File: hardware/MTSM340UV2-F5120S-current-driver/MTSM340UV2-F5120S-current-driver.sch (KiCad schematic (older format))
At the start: 9 parts

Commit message: course layout done
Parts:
- removed C?: 10V 1uF, symbol Device:C
- removed C?: 25V 3.3uF, symbol Device:C
- removed C?: 6V 1uF, symbol Device:C
- removed D?: 20V 1A, symbol Device:D_Schottky
- removed J?: LED, symbol Connector:Conn_01x02_Female
- removed L?: 22uH, symbol pspice:INDUCTOR
- removed R?: 40.2k, symbol Device:R
- removed R?: 0.665, symbol Device:R
- removed U?: LM3407MY, Package_SO:MSOP-8-1EP_3x3mm_P0.65mm_EP1.73x1.85mm_ThermalVias, symbol Regulator_Switching:LM3407MY
- added C10: 5600pF, Capacitor_SMD:C_0402_1005Metric, symbol Device:C
- added C11: 0.1uF, Capacitor_SMD:C_0402_1005Metric, symbol Device:C
- added C12: 22uF, Capacitor_SMD:C_0805_2012Metric, symbol Device:C
- added C8, C9: 2.2uF, Capacitor_SMD:C_0603_1608Metric, symbol Device:C
- added J1: LED0, Connector_PinHeader_2.54mm:PinHeader_1x02_P2.54mm_Vertical, symbol Connector:Conn_01x02_Female
- added J10: LED8, Connector_PinHeader_2.54mm:PinHeader_1x02_P2.54mm_Vertical, symbol Connector:Conn_01x02_Female
- added J11: LED9, Connector_PinHeader_2.54mm:PinHeader_1x02_P2.54mm_Vertical, symbol Connector:Conn_01x02_Female
- added J12: LED10, Connector_PinHeader_2.54mm:PinHeader_1x02_P2.54mm_Vertical, symbol Connector:Conn_01x02_Female
- added J13: LED11, Connector_PinHeader_2.54mm:PinHeader_1x02_P2.54mm_Vertical, symbol Connector:Conn_01x02_Female
- added J14: LED12, Connector_PinHeader_2.54mm:PinHeader_1x02_P2.54mm_Vertical, symbol Connector:Conn_01x02_Female
- added J15: LED13, Connector_PinHeader_2.54mm:PinHeader_1x02_P2.54mm_Vertical, symbol Connector:Conn_01x02_Female
- added J16: LED14, Connector_PinHeader_2.54mm:PinHeader_1x02_P2.54mm_Vertical, symbol Connector:Conn_01x02_Female
- added J17: LED15, Connector_PinHeader_2.54mm:PinHeader_1x02_P2.54mm_Vertical, symbol Connector:Conn_01x02_Female
- added J18: LED16, Connector_PinHeader_2.54mm:PinHeader_1x02_P2.54mm_Vertical, symbol Connector:Conn_01x02_Female
- added J19: LED17, Connector_PinHeader_2.54mm:PinHeader_1x02_P2.54mm_Vertical, symbol Connector:Conn_01x02_Female
- added J2: LED1, Connector_PinHeader_2.54mm:PinHeader_1x02_P2.54mm_Vertical, symbol Connector:Conn_01x02_Female
- added J20: LED18, Connector_PinHeader_2.54mm:PinHeader_1x02_P2.54mm_Vertical, symbol Connector:Conn_01x02_Female
- added J21: LED19, Connector_PinHeader_2.54mm:PinHeader_1x02_P2.54mm_Vertical, symbol Connector:Conn_01x02_Female
- added J22: LED20, Connector_PinHeader_2.54mm:PinHeader_1x02_P2.54mm_Vertical, symbol Connector:Conn_01x02_Female
- added J23: LED21, Connector_PinHeader_2.54mm:PinHeader_1x02_P2.54mm_Vertical, symbol Connector:Conn_01x02_Female
- added J24: LED22, Connector_PinHeader_2.54mm:PinHeader_1x02_P2.54mm_Vertical, symbol Connector:Conn_01x02_Female
- added J25: LED23, Connector_PinHeader_2.54mm:PinHeader_1x02_P2.54mm_Vertical, symbol Connector:Conn_01x02_Female
- added J26: FPC, Connector_FFC-FPC:Molex_200528-0100_1x10-1MP_P1.00mm_Horizontal, symbol Connector:Conn_01x10_Female
- added J27: POWER, Connector_BarrelJack:BarrelJack_CUI_PJ-063AH_Horizontal, symbol Connector:Conn_01x02_Female
- added J3: LED2, Connector_PinHeader_2.54mm:PinHeader_1x02_P2.54mm_Vertical, symbol Connector:Conn_01x02_Female
- added J4: LED3, Connector_PinHeader_2.54mm:PinHeader_1x02_P2.54mm_Vertical, symbol Connector:Conn_01x02_Female
- added J5: LED4, Connector_PinHeader_2.54mm:PinHeader_1x02_P2.54mm_Vertical, symbol Connector:Conn_01x02_Female
- added J6: LED5, Connector_PinHeader_2.54mm:PinHeader_1x02_P2.54mm_Vertical, symbol Connector:Conn_01x02_Female
- added J7: LED6, Connector_PinHeader_2.54mm:PinHeader_1x02_P2.54mm_Vertical, symbol Connector:Conn_01x02_Female
- added J8: LED7, Connector_PinHeader_2.54mm:PinHeader_1x02_P2.54mm_Vertical, symbol Connector:Conn_01x02_Female
- added J9: ENABLE, Connector_PinHeader_2.54mm:PinHeader_1x02_P2.54mm_Vertical, symbol Connector:Conn_01x02_Female
- added L1: 10uH, custom_lib:XAL5050-103MEC, symbol Device:L
- added MAX176321: MAX17632, custom_lib:QFN-16-1EP_3x3mm_Pitch0.5mm, symbol custom:MAX17632
- added SW1: RESET, Button_Switch_THT:SW_PUSH_6mm, symbol Switch:SW_Push
- added SW2: GPIO0, Button_Switch_THT:SW_PUSH_6mm, symbol Switch:SW_Push
- added TP8: TestPoint, TestPoint:TestPoint_Pad_D1.0mm, symbol Connector:TestPoint
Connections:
- net +12V: now also C9.1, J27.2 (Pin_2), MAX176321.1 (EN/UVLO), MAX176321.15 (Vin), MAX176321.16 (Vin)
- net GND: now also C10.2, C12.1, C8.2, C9.2, J26.1 (Pin_1), J26.2 (Pin_2), J26.7 (Pin_7), J27.1 (Pin_1), J9.1 (Pin_1), MAX176321.13 (PGND), MAX176321.14 (PGND), MAX176321.3 (SGND), MAX176321.4 (MODE/SYNC), SW1.1, SW2.1
- new net: C11.1, L1.2, MAX176321.11 (LX), MAX176321.12 (LX)
- new net: C11.2, MAX176321.10 (BST)
- new net: C8.1, MAX176321.2 (VCC)
- new net: C10.1, MAX176321.5 (SS)
- new net: J26.3 (Pin_3), SW1.2
- new net: J26.4 (Pin_4), SW2.2
- new net +5V: C12.2, J26.10 (Pin_10), J26.9 (Pin_9), L1.1, MAX176321.6 (FB), MAX176321.9 (EXTVCC), TP8.1
- new net ENABLE: J9.2 (Pin_2)
- new net LM3407-current-controller/LED+: J1.1 (Pin_1)
- new net LM3407-current-controller/LED-: J1.2 (Pin_2)
- new net PWM: J26.8 (Pin_8)
- new net RX: J26.5 (Pin_5)
- new net TX: J26.6 (Pin_6)
- new net sheet61CCCCC4/LED+: J2.1 (Pin_1)
- new net sheet61CCCCC4/LED-: J2.2 (Pin_2)
- new net sheet61CCCDBA/LED+: J3.1 (Pin_1)
- new net sheet61CCCDBA/LED-: J3.2 (Pin_2)
- new net sheet61CCCDC0/LED+: J4.1 (Pin_1)
- new net sheet61CCCDC0/LED-: J4.2 (Pin_2)
- new net sheet61CCCFC4/LED+: J5.1 (Pin_1)
- new net sheet61CCCFC4/LED-: J5.2 (Pin_2)
- new net sheet61CCCFCA/LED+: J6.1 (Pin_1)
- new net sheet61CCCFCA/LED-: J6.2 (Pin_2)
- new net sheet61CCCFD0/LED+: J7.1 (Pin_1)
- new net sheet61CCCFD0/LED-: J7.2 (Pin_2)
- new net sheet61CCCFD6/LED+: J8.1 (Pin_1)
- new net sheet61CCCFD6/LED-: J8.2 (Pin_2)
- new net sheet61CCD8EC/LED+: J10.1 (Pin_1)
- new net sheet61CCD8EC/LED-: J10.2 (Pin_2)
- new net sheet61CCD8F2/LED+: J11.1 (Pin_1)
- new net sheet61CCD8F2/LED-: J11.2 (Pin_2)
- new net sheet61CCD8F8/LED+: J12.1 (Pin_1)
- new net sheet61CCD8F8/LED-: J12.2 (Pin_2)
- new net sheet61CCD8FE/LED+: J13.1 (Pin_1)
- new net sheet61CCD8FE/LED-: J13.2 (Pin_2)
- new net sheet61CCD904/LED+: J14.1 (Pin_1)
- new net sheet61CCD904/LED-: J14.2 (Pin_2)
- new net sheet61CCD90A/LED+: J15.1 (Pin_1)
- new net sheet61CCD90A/LED-: J15.2 (Pin_2)
- new net sheet61CCD910/LED+: J16.1 (Pin_1)
- new net sheet61CCD910/LED-: J16.2 (Pin_2)
- new net sheet61CCD916/LED+: J17.1 (Pin_1)
- new net sheet61CCD916/LED-: J17.2 (Pin_2)
- new net sheet61CCE2A4/LED+: J18.1 (Pin_1)
- new net sheet61CCE2A4/LED-: J18.2 (Pin_2)
- new net sheet61CCE2AA/LED+: J19.1 (Pin_1)
- new net sheet61CCE2AA/LED-: J19.2 (Pin_2)
- new net sheet61CCE2B0/LED+: J20.1 (Pin_1)
- new net sheet61CCE2B0/LED-: J20.2 (Pin_2)
- new net sheet61CCE2B6/LED+: J21.1 (Pin_1)
- new net sheet61CCE2B6/LED-: J21.2 (Pin_2)
- new net sheet61CCE2BC/LED+: J22.1 (Pin_1)
- new net sheet61CCE2BC/LED-: J22.2 (Pin_2)
- new net sheet61CCE2C2/LED+: J23.1 (Pin_1)
- new net sheet61CCE2C2/LED-: J23.2 (Pin_2)
- new net sheet61CCE2C8/LED+: J24.1 (Pin_1)
- new net sheet61CCE2C8/LED-: J24.2 (Pin_2)
- new net sheet61CCE2CE/LED+: J25.1 (Pin_1)
- new net sheet61CCE2CE/LED-: J25.2 (Pin_2)
- no-connect marks 0 -> 2
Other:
- note removed: "0.198V/0.3A=0.66"

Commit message: layout almost done
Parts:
- removed J27: POWER, Connector_BarrelJack:BarrelJack_CUI_PJ-063AH_Horizontal, symbol Connector:Conn_01x02_Female
- removed TP8: TestPoint, TestPoint:TestPoint_Pad_D1.0mm, symbol Connector:TestPoint
- added D25: 12V, LED_SMD:LED_0603_1608Metric_Pad1.05x0.95mm_HandSolder, symbol Device:LED
- added D26: 5V, LED_SMD:LED_0603_1608Metric_Pad1.05x0.95mm_HandSolder, symbol Device:LED
- added H1, H2, H3: 12V, MountingHole:MountingHole_3.2mm_M3_DIN965_Pad_TopBottom, symbol Mechanical:MountingHole_Pad
- added H4, H5, H6: GND, MountingHole:MountingHole_3.2mm_M3_DIN965_Pad_TopBottom, symbol Mechanical:MountingHole_Pad
- added J27: Conn_01x05_Male, Connector_PinHeader_2.54mm:PinHeader_1x05_P2.54mm_Vertical, symbol Connector:Conn_01x05_Male
- added J28: UART, Connector_PinHeader_2.54mm:PinHeader_1x03_P2.54mm_Vertical, symbol Connector:Conn_01x03_Male
- added R49: 1k, Resistor_SMD:R_0603_1608Metric_Pad0.98x0.95mm_HandSolder, symbol Device:R
- added R50: 500, Resistor_SMD:R_0603_1608Metric_Pad0.98x0.95mm_HandSolder, symbol Device:R
- added R51: 150, Resistor_SMD:R_0603_1608Metric_Pad0.98x0.95mm_HandSolder, symbol Device:R
- C10: footprint Capacitor_SMD:C_0402_1005Metric -> Capacitor_SMD:C_0603_1608Metric_Pad1.08x0.95mm_HandSolder
- C11: footprint Capacitor_SMD:C_0402_1005Metric -> Capacitor_SMD:C_0805_2012Metric_Pad1.18x1.45mm_HandSolder
- C12: footprint Capacitor_SMD:C_0805_2012Metric -> Capacitor_SMD:C_0805_2012Metric_Pad1.18x1.45mm_HandSolder
- C8, C9: footprint Capacitor_SMD:C_0603_1608Metric -> Capacitor_SMD:C_0603_1608Metric_Pad1.08x0.95mm_HandSolder
- J26: footprint Connector_FFC-FPC:Molex_200528-0100_1x10-1MP_P1.00mm_Horizontal -> Connector_FFC-FPC:TE_1-84953-0_1x10-1MP_P1.0mm_Horizontal
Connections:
- net +12V: now also H1.1, H2.1, H3.1, J27.3 (Pin_3), R50.1
- net +5V: now also J27.2 (Pin_2), R51.1
- net ENABLE: now also J27.4 (Pin_4), R49.1
- net GND: now also D25.1 (K), D26.1 (K), H4.1, H5.1, H6.1, J27.1 (Pin_1), J28.1 (Pin_1), R49.2
- net PWM: now also J27.5 (Pin_5)
- net RX: now also J28.3 (Pin_3)
- net TX: now also J28.2 (Pin_2)
- new net: D25.2 (A), R50.2
- new net: D26.2 (A), R51.2

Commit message: layout done
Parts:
- added H10, H7, H8, H9: MountingHole, MountingHole:MountingHole_3.2mm_M3_DIN965, symbol Mechanical:MountingHole
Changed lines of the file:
@@
 	0    1    1    0
 $EndComp
+$Comp
+L Mechanical:MountingHole H7
+U 1 1 61DA8E40
+P 2800 2225
+F 0 "H7" H 2900 2271 50  0000 L CNN
+F 1 "MountingHole" H 2900 2180 50  0000 L CNN
+F 2 "MountingHole:MountingHole_3.2mm_M3_DIN965" H 2800 2225 50  0001 C CNN
+F 3 "~" H 2800 2225 50  0001 C CNN
+	1    2800 2225
+	1    0    0    -1
+$EndComp
+$Comp
+L Mechanical:MountingHole H8
+U 1 1 61DA9707
+P 2800 2450
+F 0 "H8" H 2900 2496 50  0000 L CNN
+F 1 "MountingHole" H 2900 2405 50  0000 L CNN
+F 2 "MountingHole:MountingHole_3.2mm_M3_DIN965" H 2800 2450 50  0001 C CNN
+F 3 "~" H 2800 2450 50  0001 C CNN
+	1    2800 2450
+	1    0    0    -1
+$EndComp
+$Comp
+L Mechanical:MountingHole H9
+U 1 1 61DAA097
+P 2800 2675
+F 0 "H9" H 2900 2721 50  0000 L CNN
+F 1 "MountingHole" H 2900 2630 50  0000 L CNN
+F 2 "MountingHole:MountingHole_3.2mm_M3_DIN965" H 2800 2675 50  0001 C CNN
+F 3 "~" H 2800 2675 50  0001 C CNN
+	1    2800 2675
+	1    0    0    -1
+$EndComp
+$Comp
+L Mechanical:MountingHole H10
+U 1 1 61DB061A
+P 2800 2900
+F 0 "H10" H 2900 2946 50  0000 L CNN
+F 1 "MountingHole" H 2900 2855 50  0000 L CNN
+F 2 "MountingHole:MountingHole_3.2mm_M3_DIN965" H 2800 2900 50  0001 C CNN
+F 3 "~" H 2800 2900 50  0001 C CNN
+	1    2800 2900
+	1    0    0    -1
+$EndComp
 $EndSCHEMATC

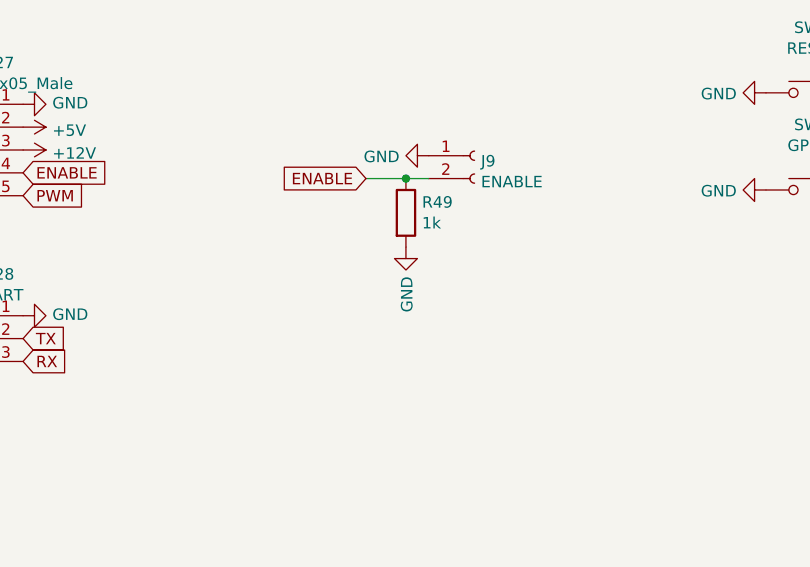
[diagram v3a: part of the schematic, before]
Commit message: with correct fpc connector and pullup on enable
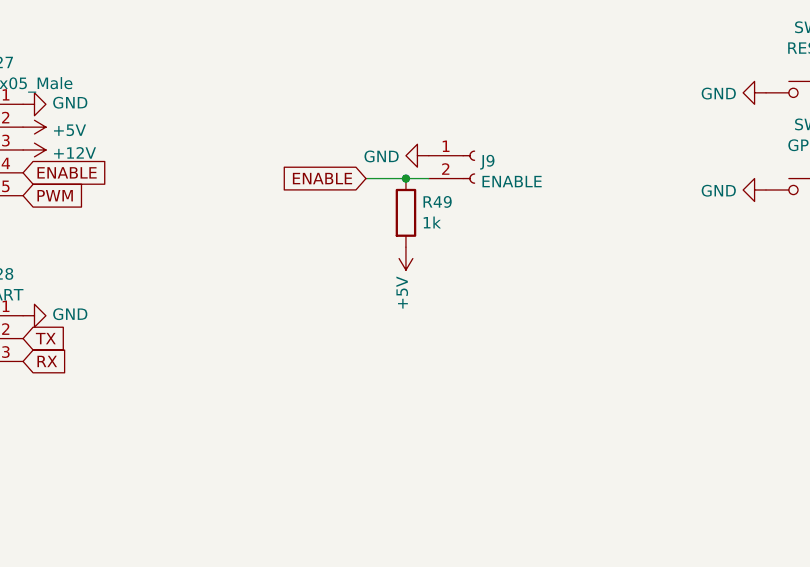
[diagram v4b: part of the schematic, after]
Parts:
- J26: footprint Connector_FFC-FPC:TE_1-84953-0_1x10-1MP_P1.0mm_Horizontal -> Connector_FFC-FPC:TE_1-1734839-0_1x10-1MP_P0.5mm_Horizontal
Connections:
- net +5V: now also R49.2
- net GND: no longer R49.2
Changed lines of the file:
@@
 F 0 "J26" H 10703 5726 50  0000 L CNN
 F 1 "FPC" H 10703 5635 50  0000 L CNN
-F 2 "Connector_FFC-FPC:TE_1-84953-0_1x10-1MP_P1.0mm_Horizontal" H 10675 5750 50  0001 C CNN
+F 2 "Connector_FFC-FPC:TE_1-1734839-0_1x10-1MP_P0.5mm_Horizontal" H 10675 5750 50  0001 C CNN
 F 3 "~" H 10675 5750 50  0001 C CNN
 	1    10675 5750
@@
 	7975 5925 8075 5925
 $Comp
-L power:GND #PWR0142
-U 1 1 61D1C982
-P 7975 6225
-F 0 "#PWR0142" H 7975 5975 50  0001 C CNN
-F 1 "GND" V 7980 6097 50  0000 R CNN
-F 2 "" H 7975 6225 50  0001 C CNN
-F 3 "" H 7975 6225 50  0001 C CNN
-	1    7975 6225
-	1    0    0    -1
-$EndComp
-$Comp
 L Connector:Conn_01x03_Male J28
 U 1 1 61D47439
@@
 	1    0    0    -1
 $EndComp
+$Comp
+L power:+5V #PWR?
+U 1 1 61D066E9
+P 7975 6225
+F 0 "#PWR?" H 7975 6075 50  0001 C CNN
+F 1 "+5V" V 7990 6353 50  0000 L CNN
+F 2 "" H 7975 6225 50  0001 C CNN
+F 3 "" H 7975 6225 50  0001 C CNN
+	1    7975 6225
+	-1   0    0    1
+$EndComp
 $EndSCHEMATC
